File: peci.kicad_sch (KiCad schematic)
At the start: 14 parts, among them Q1401 PJE138K, U1401 MAX6621AUB, U1402 TXS0102DQER

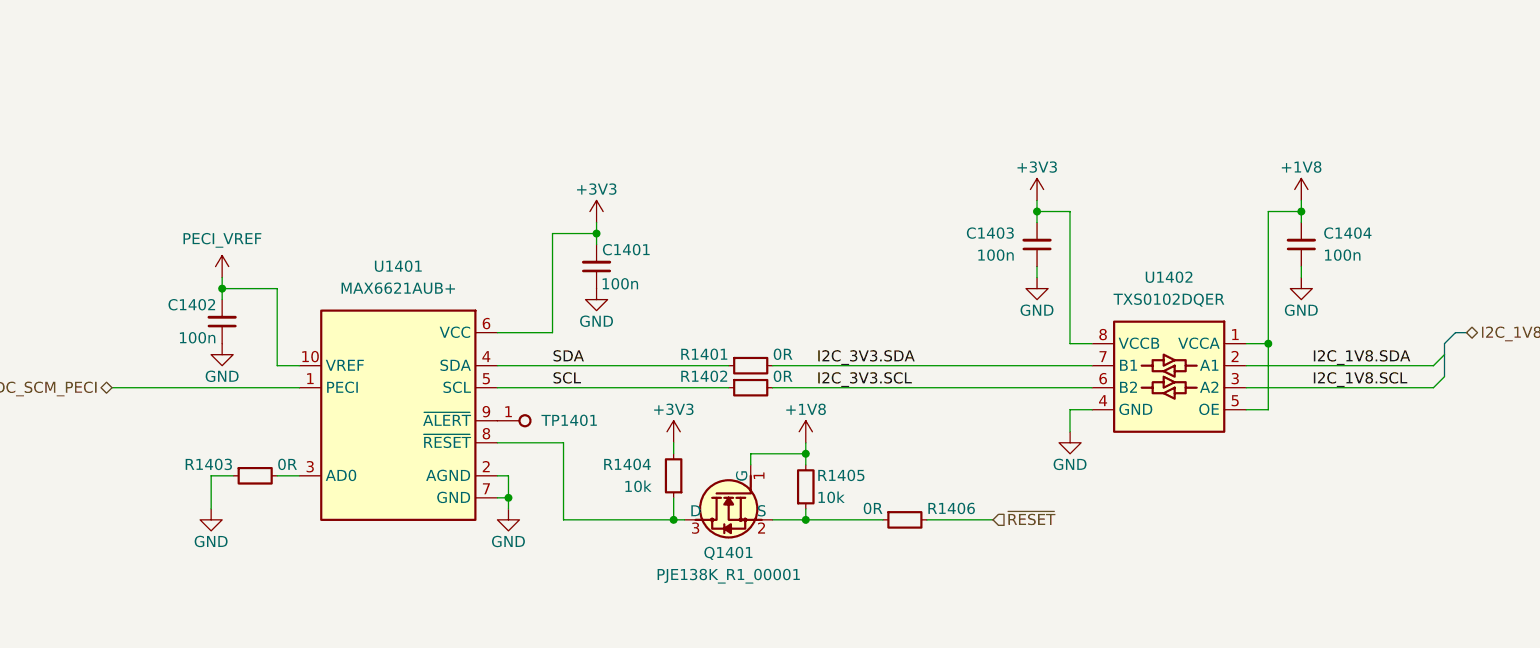
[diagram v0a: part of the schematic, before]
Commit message: [#100501] Add optional pullup for PECI address pin, add note about its address and translator having internal pullups
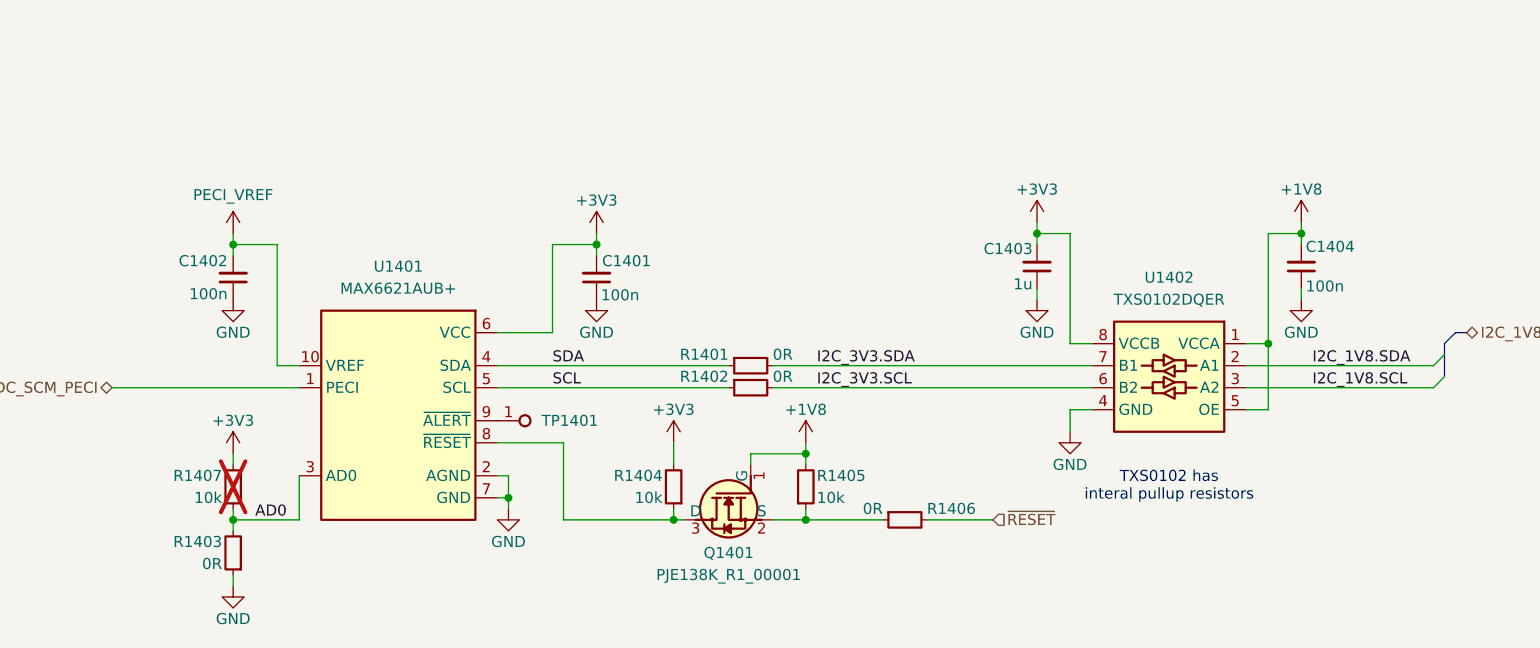
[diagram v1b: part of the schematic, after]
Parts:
- removed C1403: C_100n_0402, antmicro-footprints:C_0402_1005Metric, symbol antmicroCapacitors0402:C_100n_0402
- added C1403: C_1u_0402, antmicro-footprints:C_0402_1005Metric, symbol antmicroCapacitors0402:C_1u_0402
- added R1407: R_10k_0402, antmicro-footprints:R_0402_1005Metric, symbol antmicroResistors0402:R_10k_0402
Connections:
- net +3V3: now also C1403.2, R1407.2
- net GND: now also C1403.1
- net AD0: now reaches R1403.2, U1401.3 (AD0)
- net AD0: now also R1407.1
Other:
- note added: "TXS0102 has interal pullup resistors"
- moved on the sheet: C1401, C1402, C1404, R1404

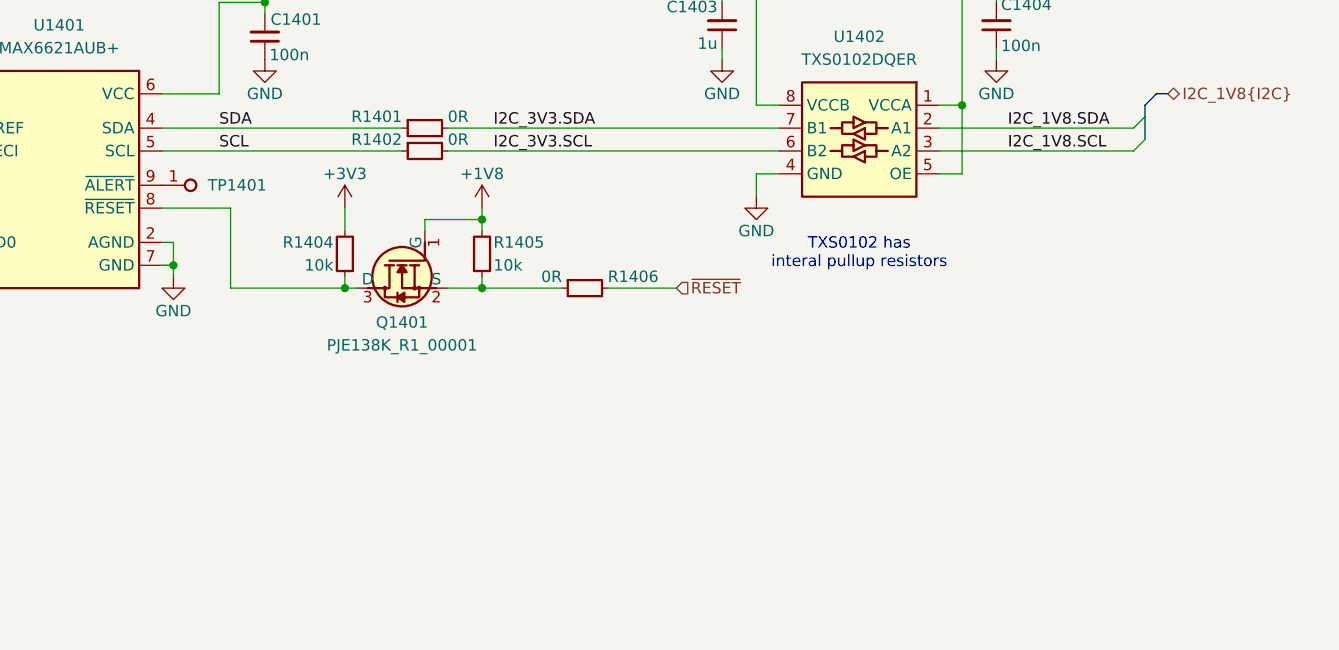
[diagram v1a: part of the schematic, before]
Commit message: [#100501] Connect PECI ALERT to FPGA HVIO pin
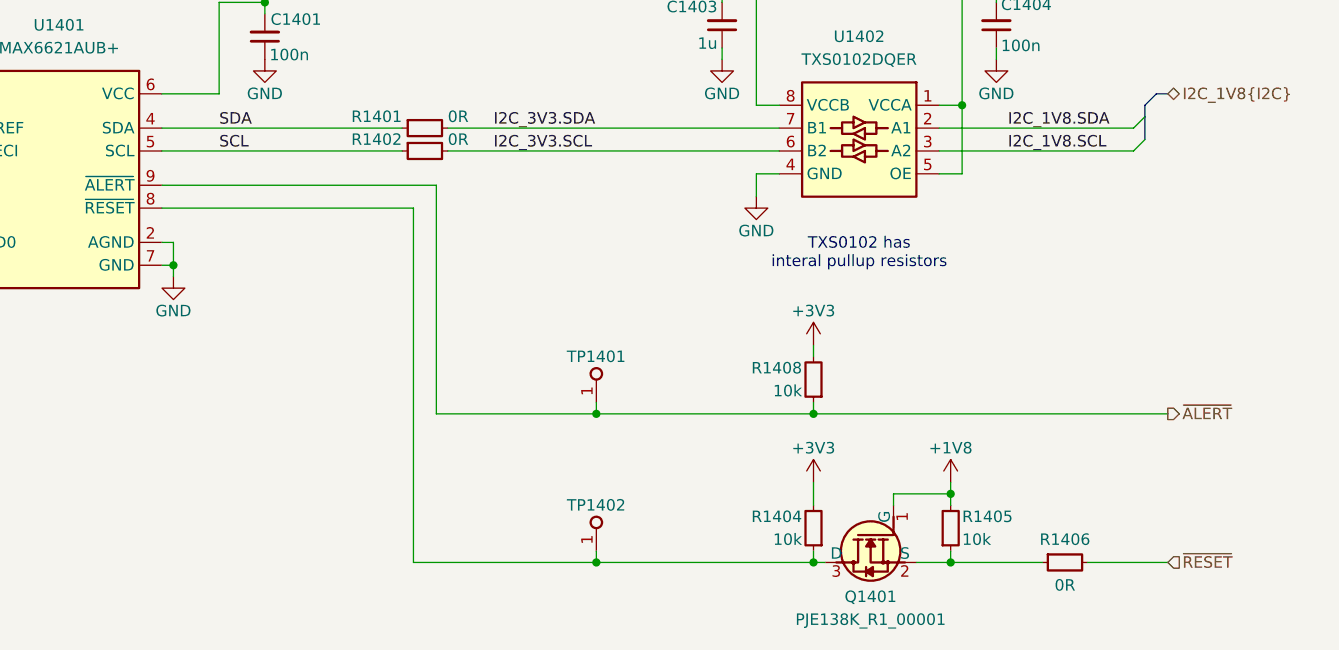
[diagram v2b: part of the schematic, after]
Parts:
- added R1408: R_10k_0402, antmicro-footprints:R_0402_1005Metric, symbol antmicroResistors0402:R_10k_0402
- added TP1402: TP_0.75mm_SMD, antmicro-footprints:TP_SMD_0.75mm, symbol antmicroTestPoints:TP_0.75mm_SMD
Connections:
- net +3V3: now also R1408.2
- net at Q1401.3 (D), R1404.1, U1401.8 (~{RESET}): now also TP1402.1
- net ~{ALERT}: now reaches TP1401.1, U1401.9 (~{ALERT})
- net ~{ALERT}: now also R1408.1
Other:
- moved on the sheet: Q1401, R1404, R1405, R1406

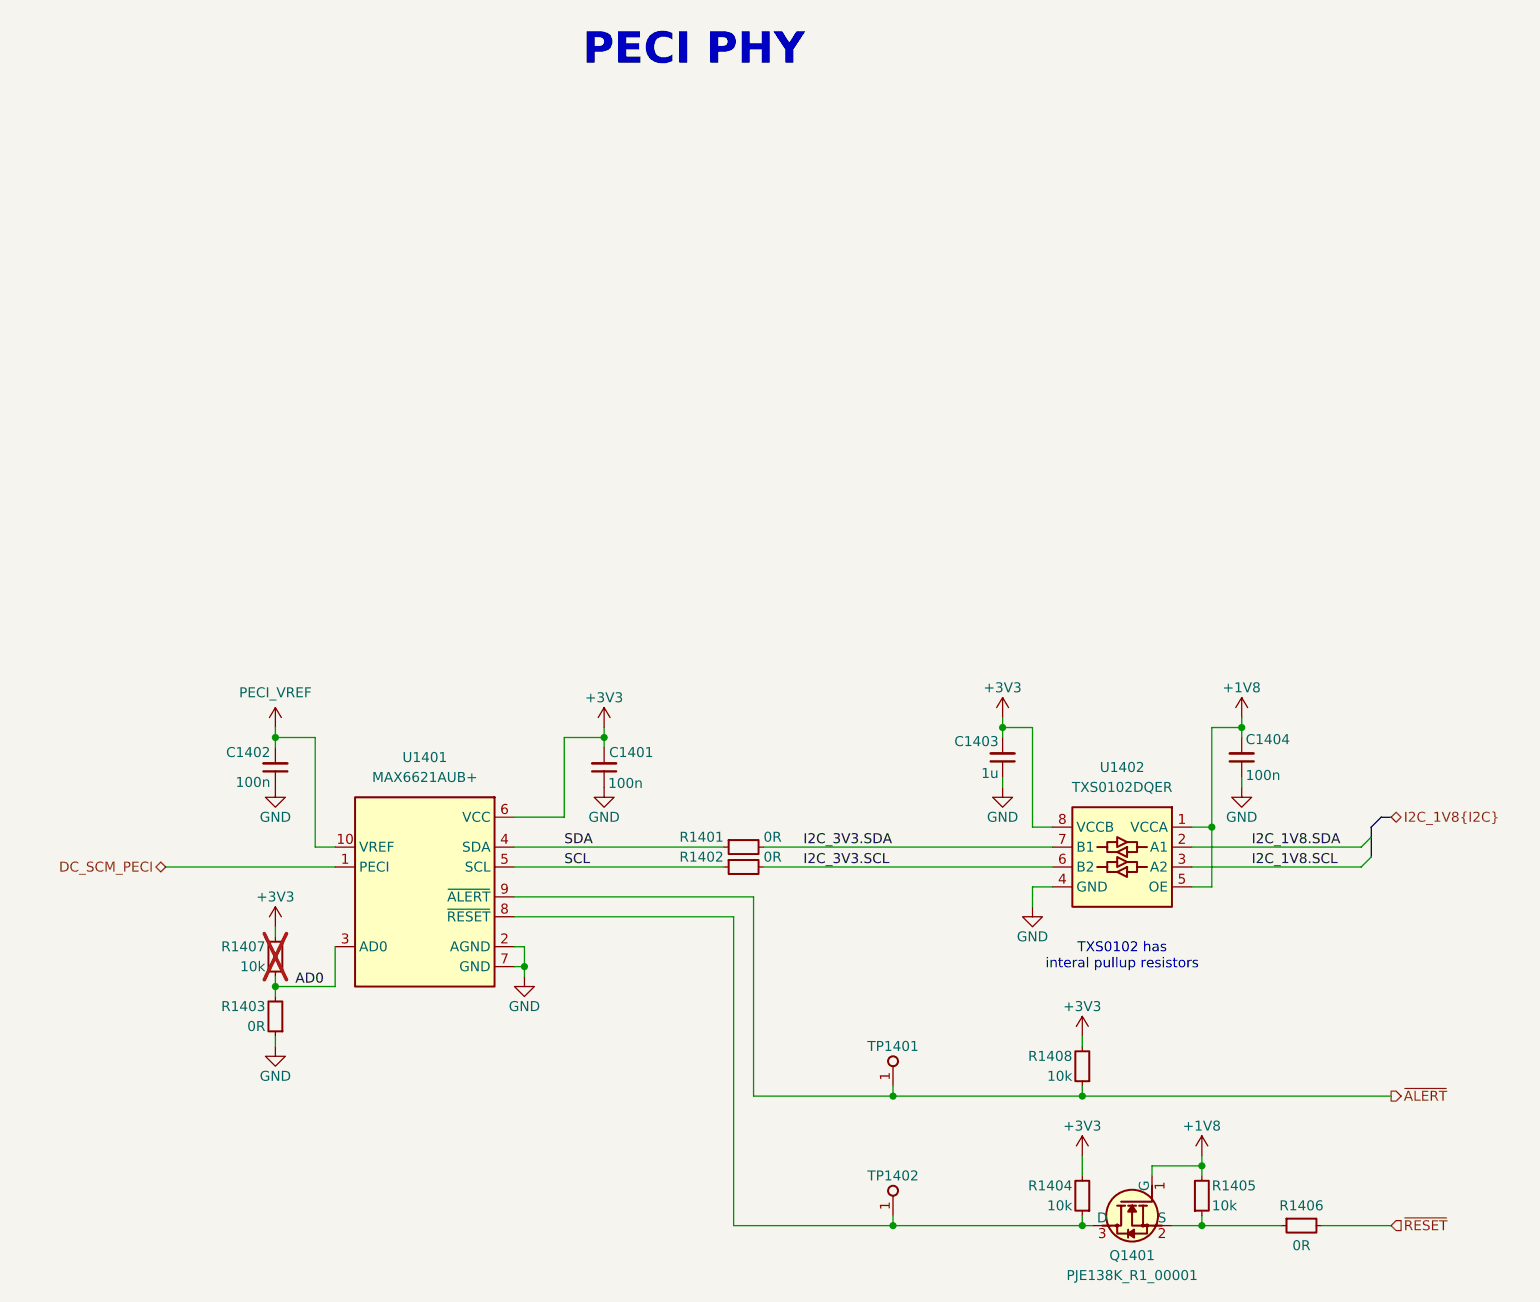
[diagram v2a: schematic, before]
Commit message: [#100501] Add test point to PECI, PECI_VREF, SDA and SCL
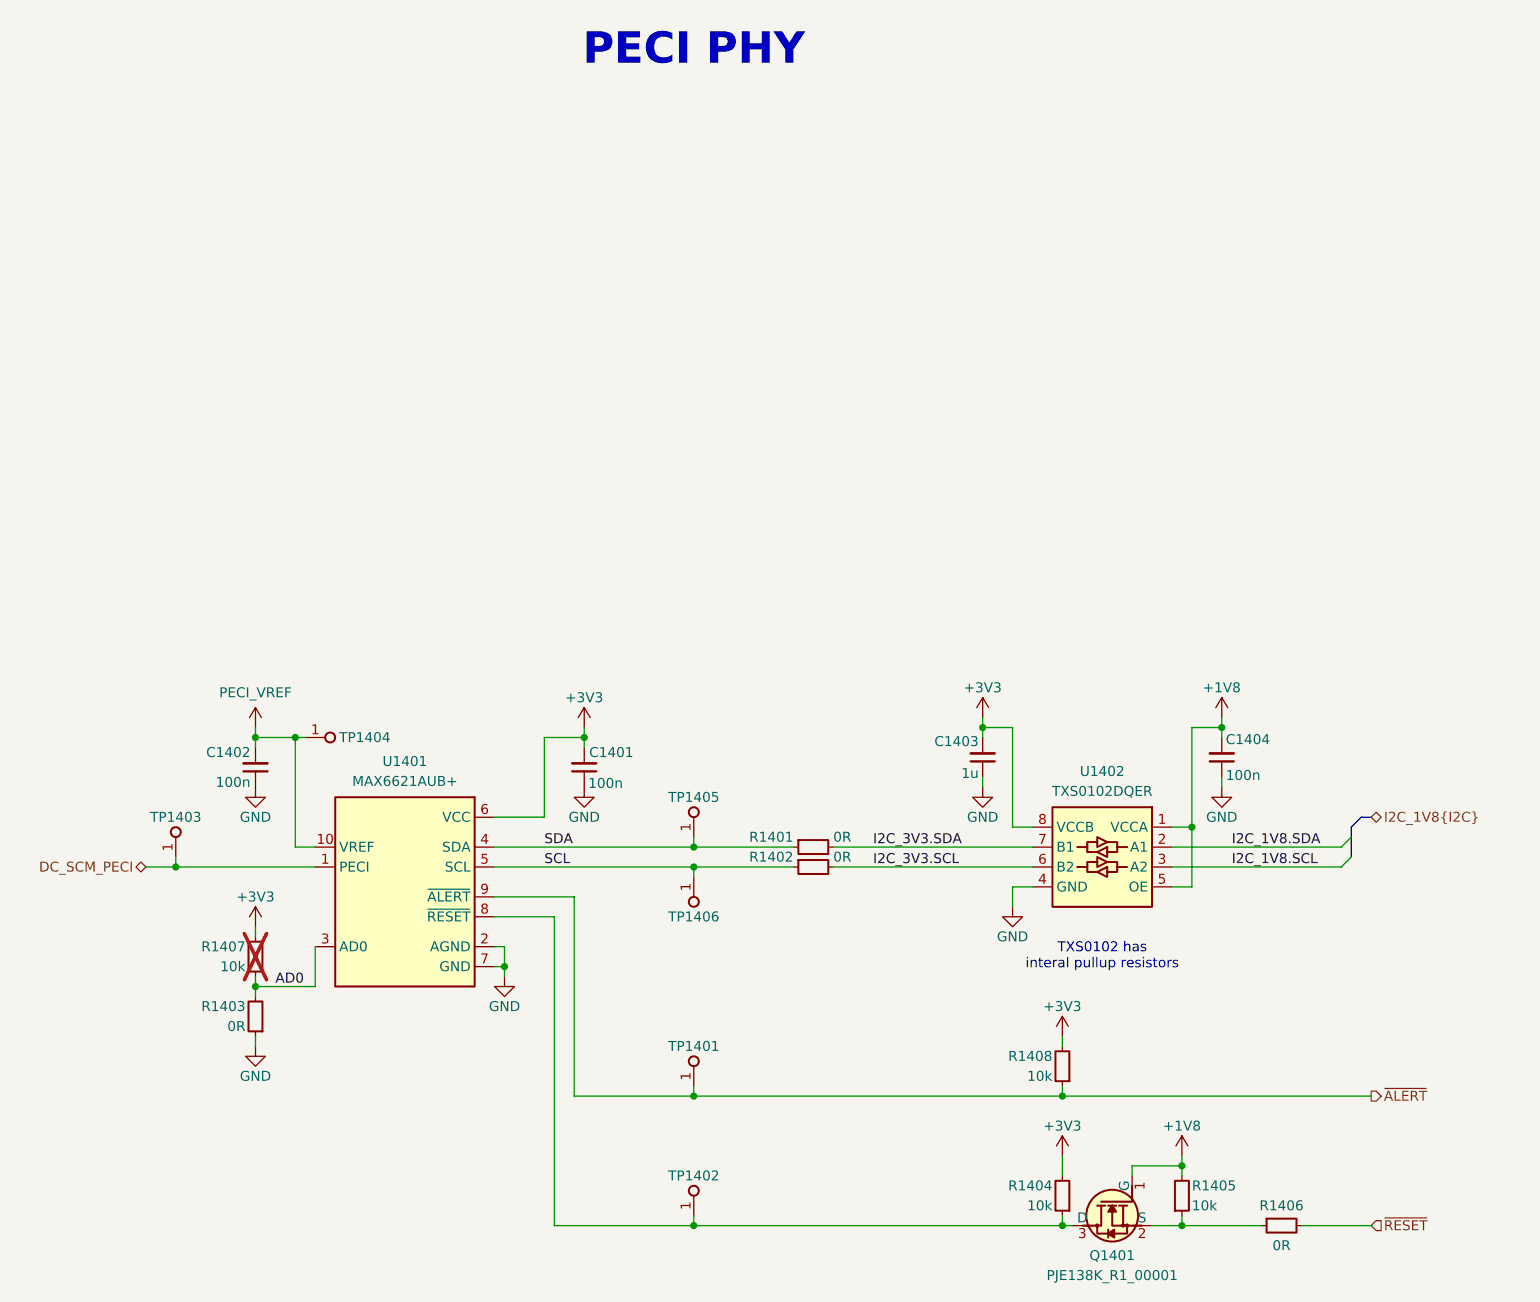
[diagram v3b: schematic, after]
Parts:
- added TP1403, TP1404, TP1405, TP1406: TP_0.75mm_SMD, antmicro-footprints:TP_SMD_0.75mm, symbol antmicroTestPoints:TP_0.75mm_SMD
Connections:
- net DC_SCM_PECI: now also TP1403.1
- net PECI_VREF: now also TP1404.1
- net SCL: now also TP1406.1
- net SDA: now also TP1405.1
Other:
- moved on the sheet: C1401, C1402, C1403, C1404, Q1401, R1401, R1402, R1403, R1404, R1405, R1406, R1407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

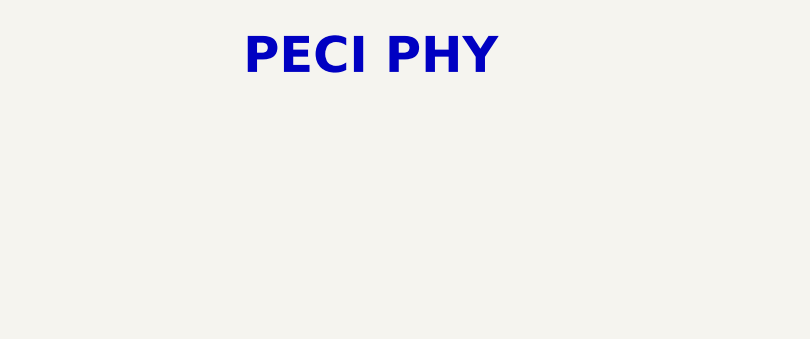
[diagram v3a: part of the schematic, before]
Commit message: [#100282] Add missing schematic sheet names and align them all
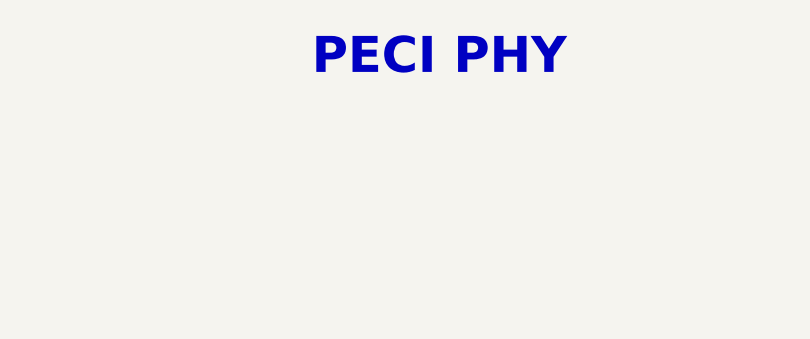
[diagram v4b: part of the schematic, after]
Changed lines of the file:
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@@
 	(text "PECI PHY"
 		(exclude_from_sim no)
-		(at 203.2 38.1 0)
+		(at 210.82 38.1 0)
 		(effects
 			(font

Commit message: [#100501] Reannotate schematic
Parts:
- renumbered C1403 to C101, C1404 to C102, C1402 to C103, C1401 to C104, Q1401 to Q1, R1401 to R145, R1402 to R146, R1407 to R147, R1403 to R148, R1408 to R149, R1404 to R150, R1405 to R151, R1406 to R152, TP1404 to TP14, TP1405 to TP15, TP1403 to TP16, TP1406 to TP17, TP1401 to TP18, TP1402 to TP19, U1402 to U17, U1401 to U18
